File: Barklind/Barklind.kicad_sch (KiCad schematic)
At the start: 3 parts, among them M1 Fan_Tacho_PWM, M2 Fan_Tacho_PWM, M3 Fan_Tacho_PWM

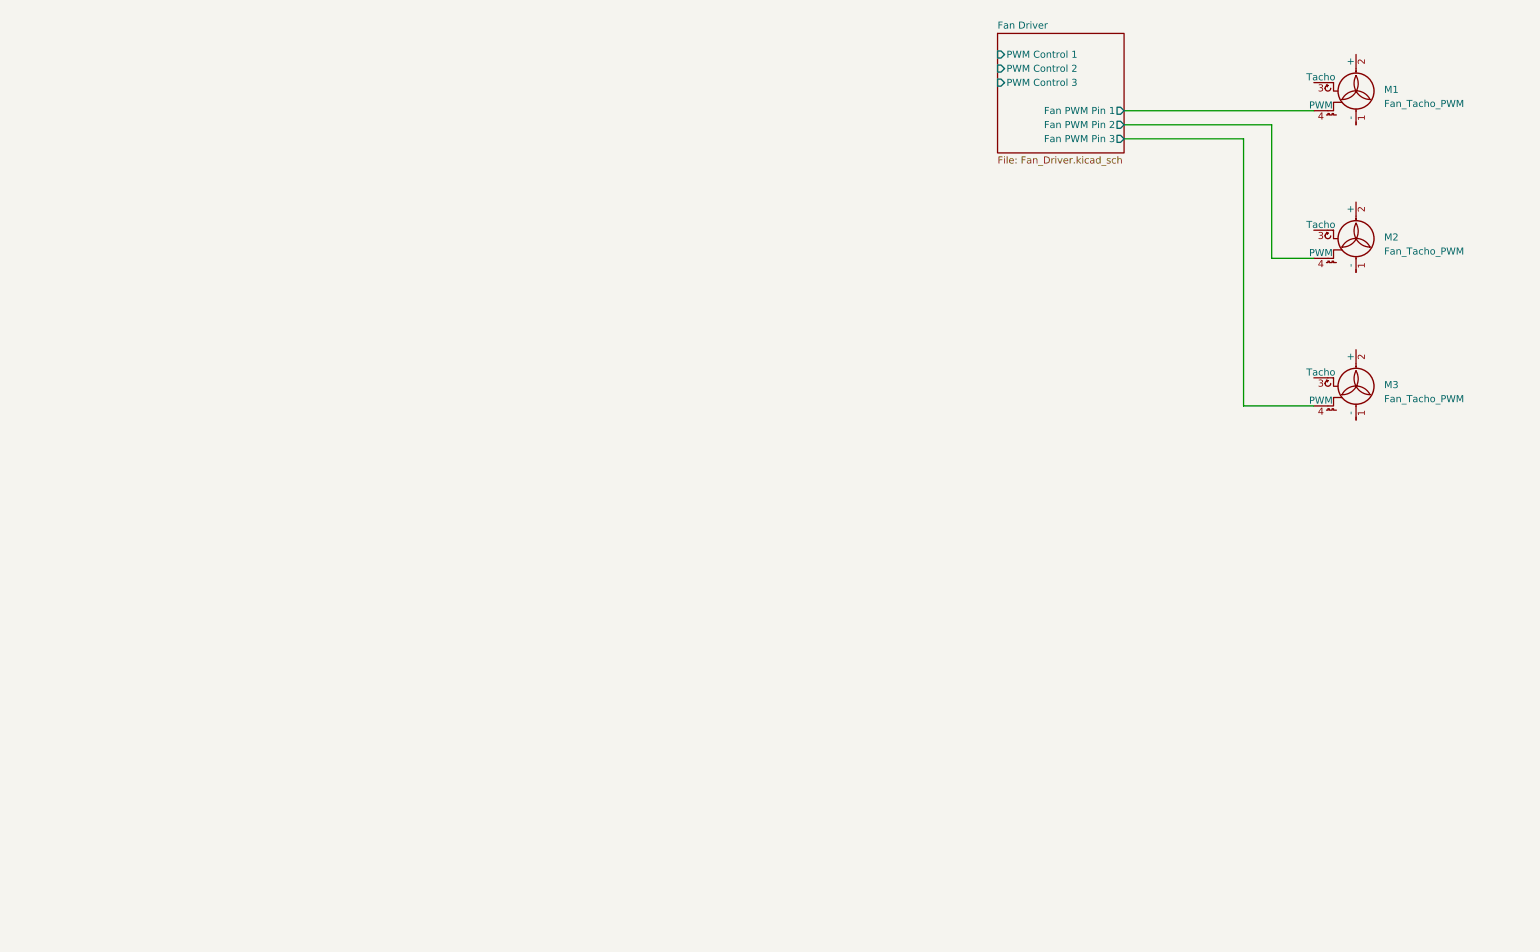
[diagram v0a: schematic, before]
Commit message: Added PoE Hierarchical sheet Added RJ45 connector with PoE support Changed from fans in schematic to generic 4 pin connectors
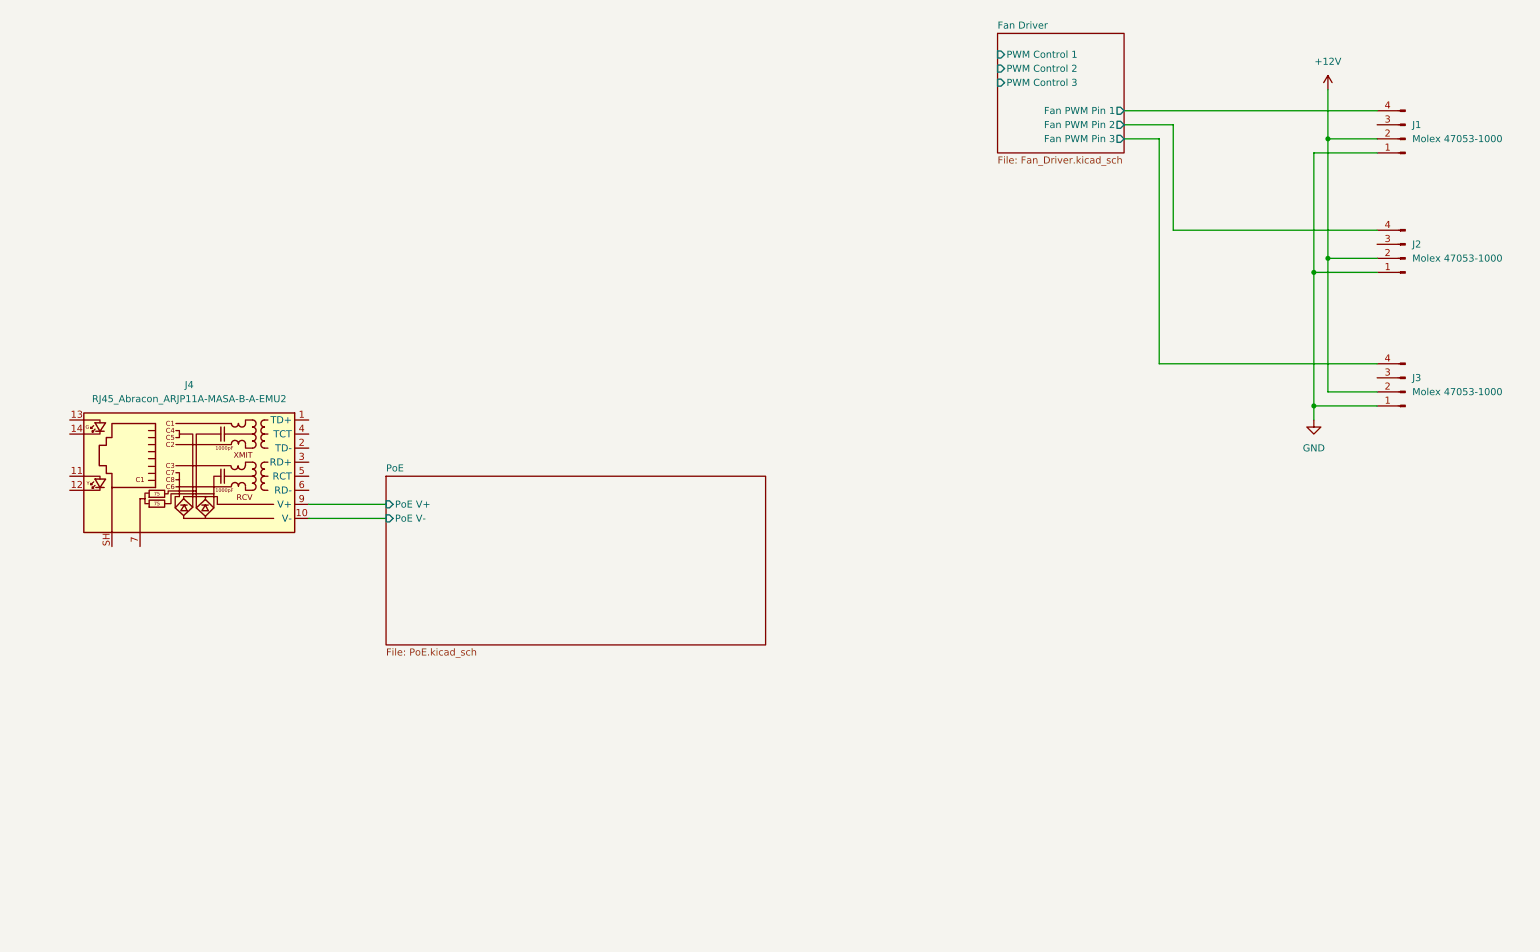
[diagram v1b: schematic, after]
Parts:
- removed M1, M2, M3: Fan_Tacho_PWM, symbol Motor:Fan_Tacho_PWM
- added J1, J2, J3: Molex 47053-1000, symbol Connector:Conn_01x04_Pin
- added J4: RJ45_Abracon_ARJP11A-MASA-B-A-EMU2, Connector_RJ:RJ45_Abracon_ARJP11A-MA_Horizontal, symbol Connector:RJ45_Abracon_ARJP11A-MASA-B-A-EMU2
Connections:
- net Fan Driver/Fan PWM Pin 1: now also J1.4 (Pin_4)
- net Fan Driver/Fan PWM Pin 2: now also J2.4 (Pin_4)
- net Fan Driver/Fan PWM Pin 3: now also J3.4 (Pin_4)
- new net +12V: J1.2 (Pin_2), J2.2 (Pin_2), J3.2 (Pin_2)
- new net GND: J1.1 (Pin_1), J2.1 (Pin_1), J3.1 (Pin_1)
- new net PoE/PoE V+: J4.9 (V+)
- new net PoE/PoE V-: J4.10 (V-)
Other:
- added sheet PoE (PoE.kicad_sch)

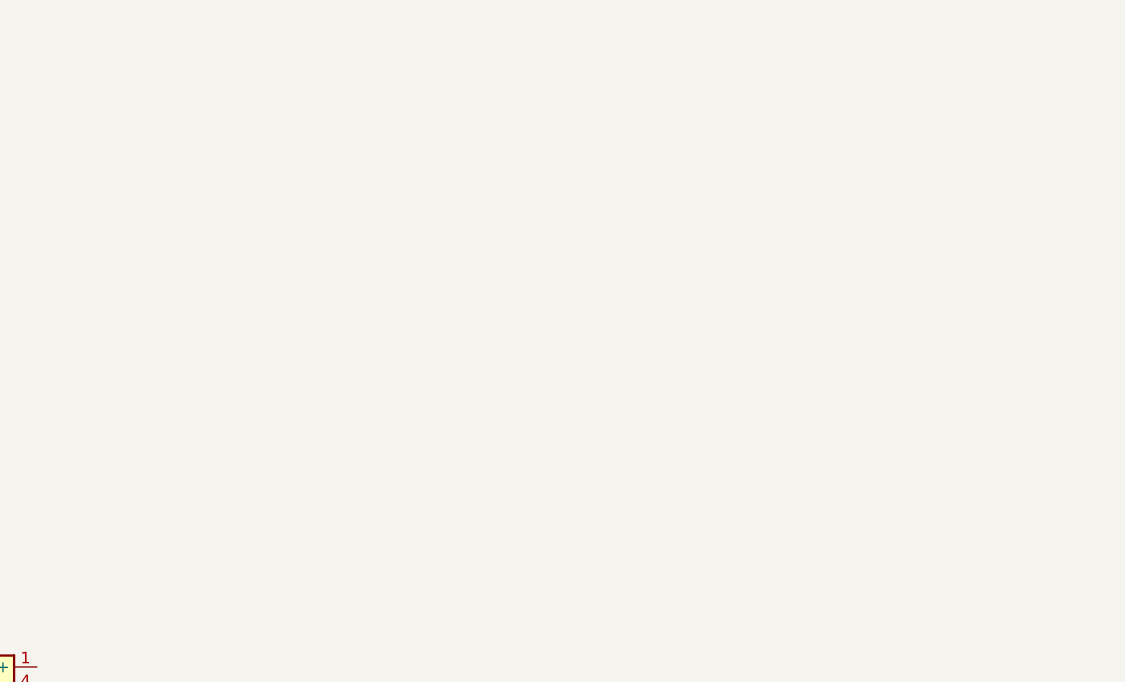
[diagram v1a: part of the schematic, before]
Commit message: Added Ethercat schematic Added W5500 to component suggestions Added picture to explain CD4007UB wiring
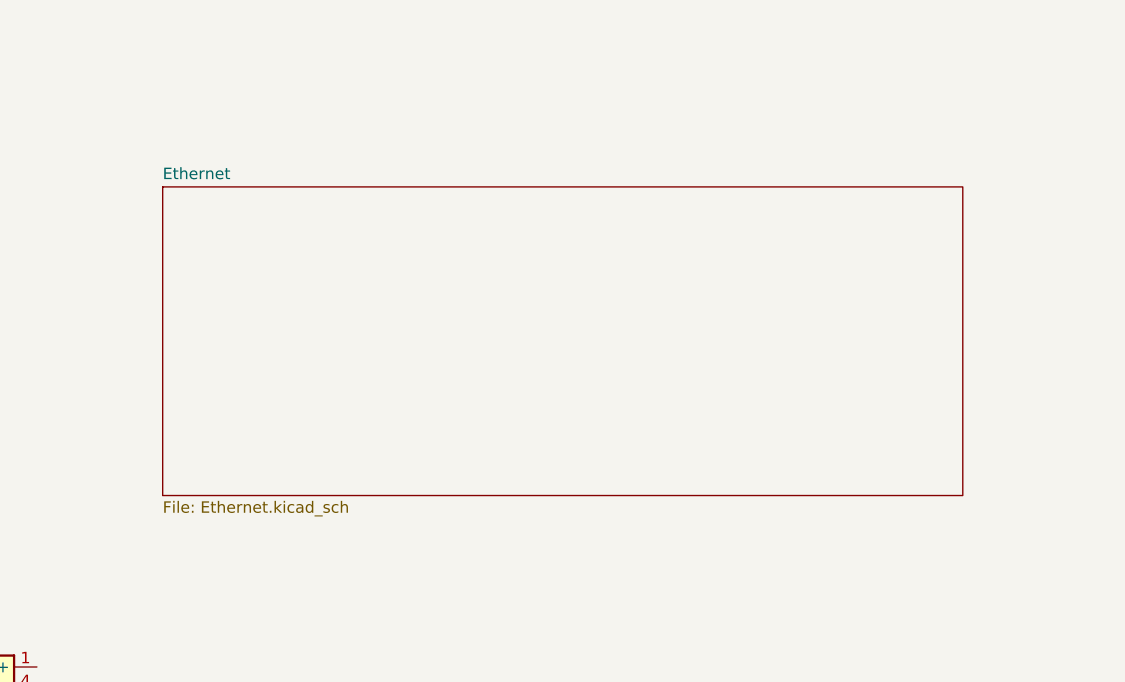
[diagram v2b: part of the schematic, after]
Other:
- added sheet Ethernet (Ethernet.kicad_sch)
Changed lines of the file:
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@@
+	)
+	(sheet
+		(at 80.01 45.72)
+		(size 88.9 34.29)
+		(fields_autoplaced yes)
+		(stroke
+			(width 0.1524)
+			(type solid)
+		)
+		(fill
+			(color 0 0 0 0.0000)
+		)
+		(property "Sheetname" "Ethernet"
+			(at 80.01 45.0084 0)
+			(effects
+				(font
+					(size 1.27 1.27)
+				)
+				(justify left bottom)
+			)
+		)
+		(property "Sheetfile" "Ethernet.kicad_sch"
+			(at 80.01 80.5946 0)
+			(effects
+				(font
+					(size 1.27 1.27)
+				)
+				(justify left top)
+			)
+		)
+		(instances
+			(project "Barklind"
+				(path "/489e2a6e-50ed-4353-8289-8893922fad24"
+					(page "4")
+				)
+			)
+		)
 	)
 	(sheet

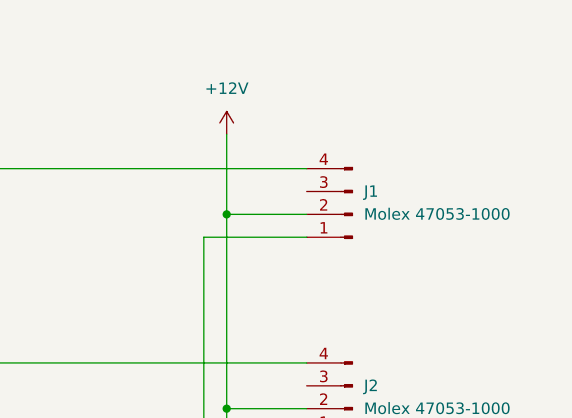
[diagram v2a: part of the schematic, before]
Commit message: Added comment on schematic to test workflow export
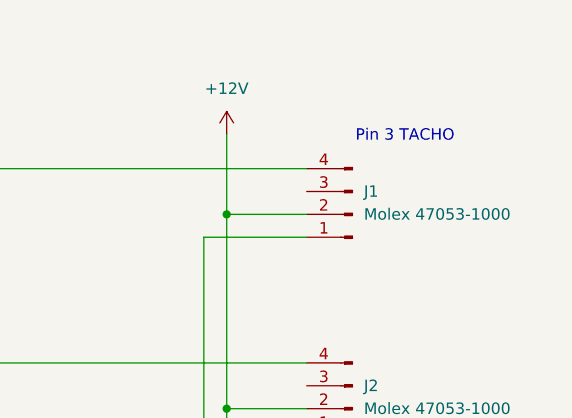
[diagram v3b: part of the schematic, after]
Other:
- note added: "Pin 3 TACHO"
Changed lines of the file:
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@@
+		)
+	)
+	(text "Pin 3 TACHO"
+		(exclude_from_sim no)
+		(at 270.002 39.624 0)
+		(effects
+			(font
+				(size 1.27 1.27)
+			)
 		)
 	)

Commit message: Comment for testing
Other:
- note added: "Placeholder"
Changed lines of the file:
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@@
+		)
+	)
+	(text "Placeholder"
+		(exclude_from_sim no)
+		(at 41.656 127.254 0)
+		(effects
+			(font
+				(size 1.27 1.27)
+			)
 		)
 	)

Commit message: Added another comment to schematic for workflow testing
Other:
- note added: "What version of ESP32?"
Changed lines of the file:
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@@
+		)
+	)
+	(text "What version of ESP32?"
+		(exclude_from_sim no)
+		(at 92.964 171.196 0)
+		(effects
+			(font
+				(size 1.27 1.27)
+			)
 		)
 	)
